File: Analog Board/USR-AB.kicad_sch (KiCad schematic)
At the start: 6 parts, among them J2 S5B-XH-A_LF__SN_, J3 S5B-XH-A_LF__SN_, U2 CD74HC4067SM96, U3 SC0918

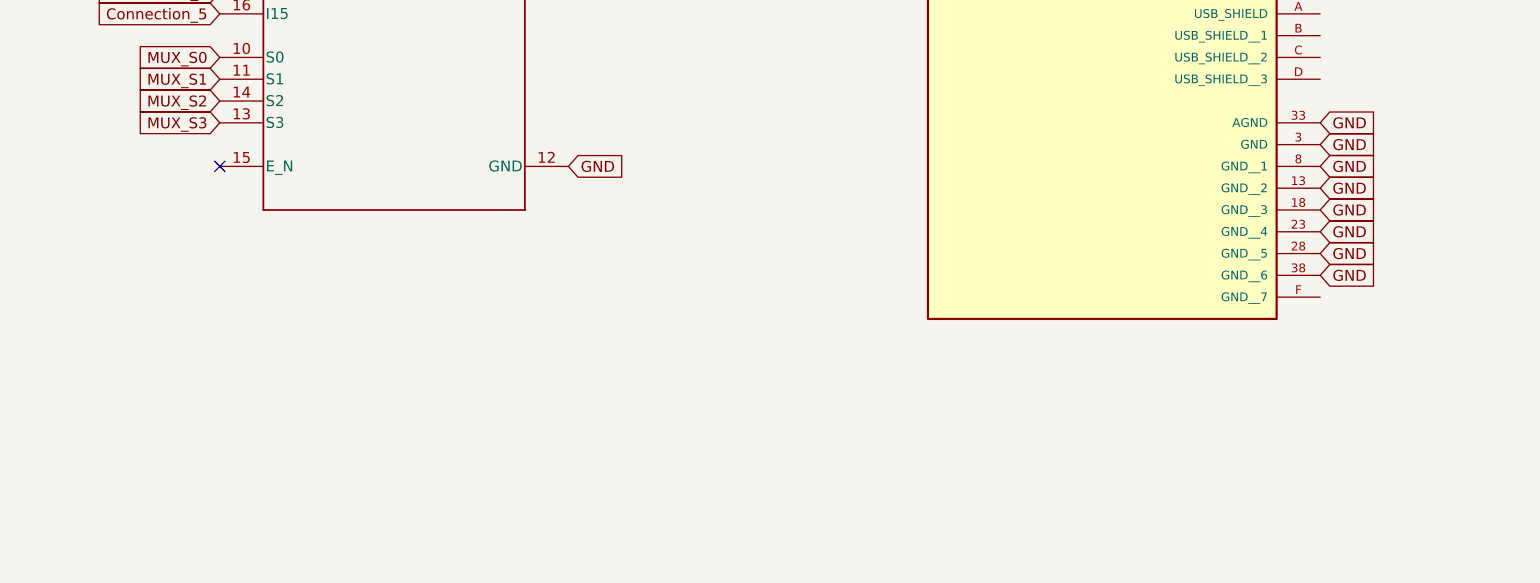
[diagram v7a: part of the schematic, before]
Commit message: Updated PCB designs across the motor driver, analog board, and PDB
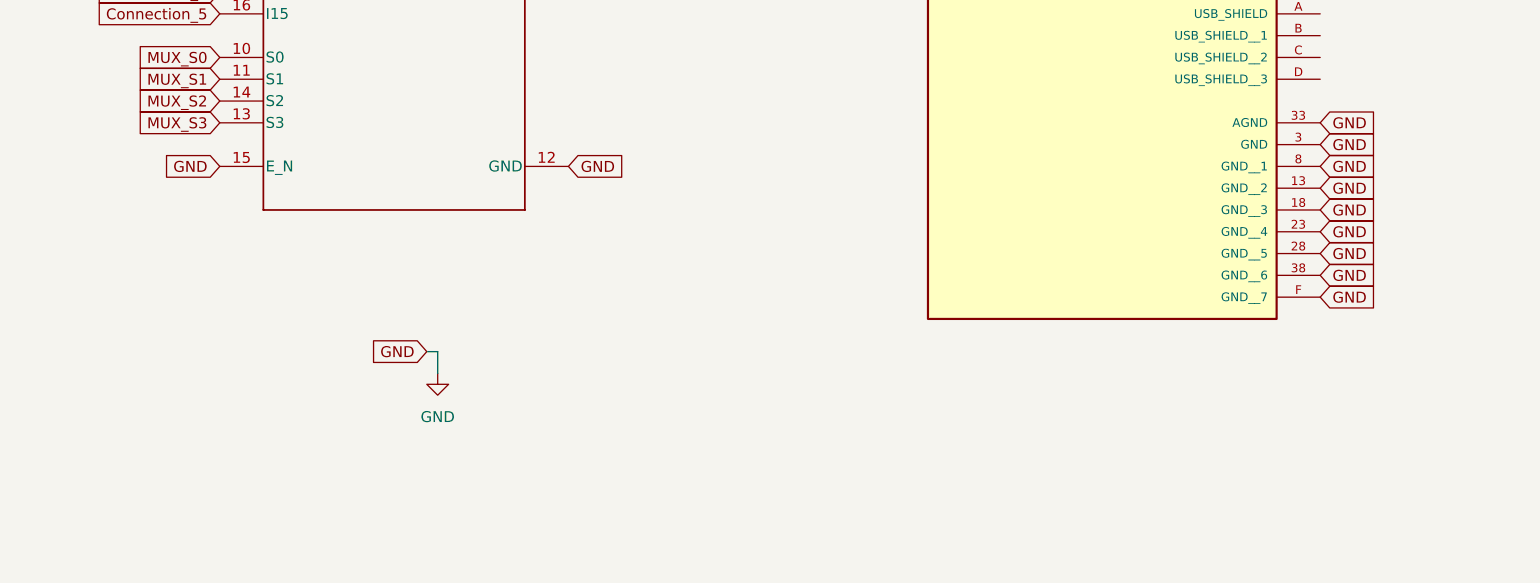
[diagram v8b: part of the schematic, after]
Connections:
- net GND: now also U2.15 (E_N), U3.F (GND__7)
- no-connect marks 1 -> 0
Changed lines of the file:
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@@
 		)
 	)
-	(no_connect
-		(at 149.86 214.63)
+	(wire
+		(pts
+			(xy 175.26 238.76) (xy 175.26 236.22)
+		)
+		(stroke
+			(width 0)
+			(type default)
+		)
+	)
+	(wire
+		(pts
+			(xy 175.26 236.22) (xy 173.99 236.22)
+		)
+		(stroke
+			(width 0)
+			(type default)
+		)
 	)
 	(global_label "M3_CS"
@@
 		)
 	)
+	(global_label "GND"
+		(shape input)
+		(at 173.99 236.22 180)
+		(fields_autoplaced yes)
+		(effects
+			(font
+				(size 1.27 1.27)
+			)
+			(justify right)
+		)
+		(property "Intersheetrefs" "${INTERSHEET_REFS}"
+			(at 167.1343 236.22 0)
+			(hide yes)
+			(show_name no)
+			(do_not_autoplace no)
+			(effects
+				(font
+					(size 1.27 1.27)
+				)
+				(justify right)
+			)
+		)
+	)
 	(global_label "MUX_S0"
 		(shape input)
@@
 	(global_label "GND"
 		(shape input)
+		(at 278.13 229.87 0)
+		(fields_autoplaced yes)
+		(effects
+			(font
+				(size 1.27 1.27)
+			)
+			(justify left)
+		)
+		(property "Intersheetrefs" "${INTERSHEET_REFS}"
+			(at 284.9857 229.87 0)
+			(hide yes)
+			(show_name no)
+			(do_not_autoplace no)
+			(effects
+				(font
+					(size 1.27 1.27)
+				)
+				(justify left)
+			)
+		)
+	)
+	(global_label "GND"
+		(shape input)
 		(at 54.61 186.69 180)
 		(fields_autoplaced yes)
@@
 		(property "Intersheetrefs" "${INTERSHEET_REFS}"
 			(at 144.78 124.905 90)
+			(hide yes)
+			(show_name no)
+			(do_not_autoplace no)
+			(effects
+				(font
+					(size 1.27 1.27)
+				)
+				(justify right)
+			)
+		)
+	)
+	(global_label "GND"
+		(shape input)
+		(at 149.86 214.63 180)
+		(fields_autoplaced yes)
+		(effects
+			(font
+				(size 1.27 1.27)
+			)
+			(justify right)
+		)
+		(property "Intersheetrefs" "${INTERSHEET_REFS}"
+			(at 143.0043 214.63 0)
 			(hide yes)
 			(show_name no)
@@
 					(unit 1)
 				)
+			)
+		)
+	)
+	(symbol
+		(lib_id "power:GND")
+		(at 175.26 238.76 0)
+		(unit 1)
+		(body_style 1)
+		(exclude_from_sim no)
+		(in_bom yes)
+		(on_board yes)
+		(in_pos_files yes)
+		(dnp no)
+		(fields_autoplaced yes)
+		(property "Reference" "#PWR01"
+			(at 175.26 245.11 0)
+			(hide yes)
+			(show_name no)
+			(do_not_autoplace no)
+			(effects
+				(font
+					(size 1.27 1.27)
+				)
+			)
+		)
+		(property "Value" "GND"
+			(at 175.26 243.84 0)
+			(show_name no)
+			(do_not_autoplace no)
+			(effects
+				(font
+					(size 1.27 1.27)
+				)
+			)
+		)
+		(property "Footprint" ""
+			(at 175.26 238.76 0)
+			(hide yes)
+			(show_name no)
+			(do_not_autoplace no)
+			(effects
+				(font
+					(size 1.27 1.27)
+				)
+			)
+		)
+		(property "Datasheet" ""
+			(at 175.26 238.76 0)
+			(hide yes)
+			(show_name no)
+			(do_not_autoplace no)
+			(effects
+				(font
+					(size 1.27 1.27)
+				)
+			)
+		)
+		(property "Description" "Power symbol creates a global label with name \"GND\" , ground"
+			(at 175.26 238.76 0)
+			(hide yes)
+			(show_name no)
+			(do_not_autoplace no)
+			(effects
+				(font
+					(size 1.27 1.27)
+				)
+			)
+		)
+		(pin "1"
+		)
+		(instances
+			(project "USR-AB"
+				(path "/08fc82fb-454e-480f-a944-ad7b66725a36"
+					(reference "#PWR01")
+					(unit 1)
+				)
